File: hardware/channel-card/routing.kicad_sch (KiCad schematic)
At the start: 37 parts, among them J301 AUX1 PRE 1-3/2-4, POST 3-5/4-6, J302 AUX2 PRE 1-3/2-4, POST 3-5/4-6, Q301 MMBT3904, SW301 PFL (latching), SW302 SC SEND (latching), SW303 COMP BUS (latching), U301 NE5532, U302 DG413DY, U303 DG412DY

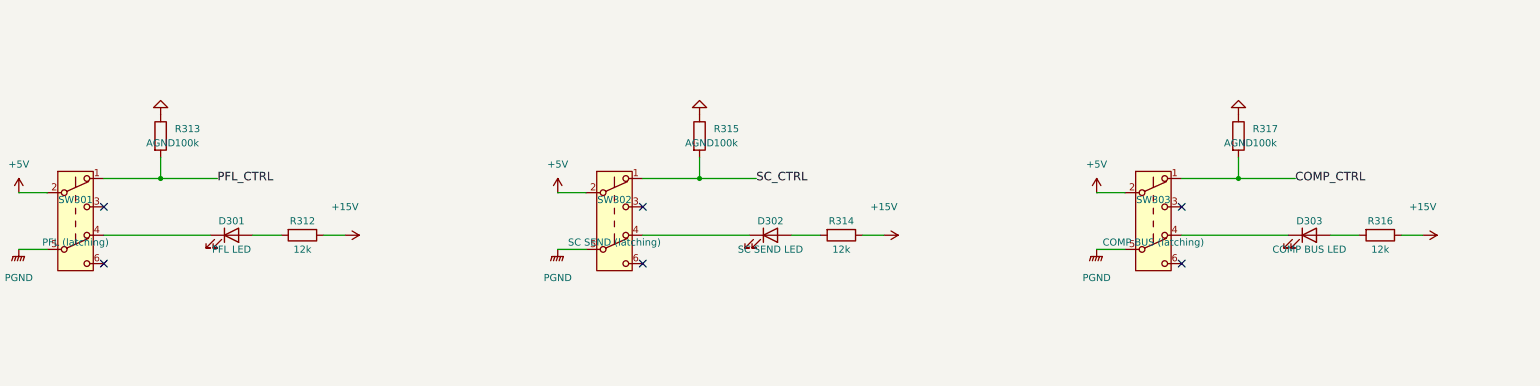
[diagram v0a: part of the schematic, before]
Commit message: Choose GPBS850N latching buttons with printed light caps
Buttons are CW Industries GPBS850N latching DPDT switches (Electrokit)
with 0805 LEDs lighting 3D-printed translucent caps (decision 75).
The datasheet shows pins 2-3 and 5-6 close when pressed, so every
button now uses pin 3 for logic and pin 6 for the LED. Adds the switch
footprint library, rebuild_all.sh, the state-retention requirement for
the momentary-button backlog item, and ten switches to the second
Electrokit order.

Co-Authored-By: Claude Opus 5.5 <noreply@anthropic.com>
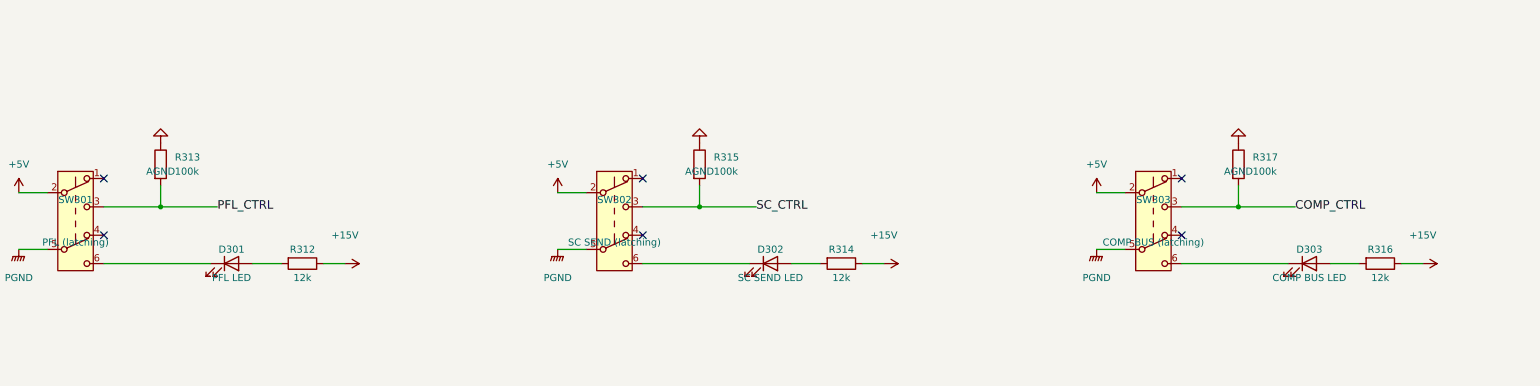
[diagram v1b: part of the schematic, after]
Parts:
- D301, D302, D303: footprint LED_THT:LED_D3.0mm -> LED_SMD:LED_0805_2012Metric
- SW301, SW302, SW303: footprint (none) -> syntsamix:SW_Latching_8.5x8.5mm_CW_GPBS850N; MPN (none) -> GPBS850N; Manufacturer (none) -> CW Industries; Supplier (none) -> Electrokit; SupplierPN (none) -> 41012905
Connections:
- net COMP_CTRL: now also SW303.3 (C); no longer SW303.1 (A)
- net PFL_CTRL: now also SW301.3 (C); no longer SW301.1 (A)
- net SC_CTRL: now also SW302.3 (C); no longer SW302.1 (A)
- net at SW301.4 (A): no longer D301.1 (K)
- net at D303.1 (K): now also SW303.6 (C); no longer SW303.4 (A)
- net at D302.1 (K): now also SW302.6 (C); no longer SW302.4 (A)
- net at SW301.6 (C): now also D301.1 (K)

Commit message: Add test pads to the channel card sheets
24 bare 1.5 mm test pads on key audio, control and ground nets across
the Input, Filter, Level, Routing and Meter sheets, named by net and
kept out of the BOM (decision 77). Each pad is in the reference
netlists, so the checks prove it sits on the intended net.

Co-Authored-By: Claude Opus 5.5 <noreply@anthropic.com>
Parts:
- added TP301: L_PRE, TestPoint:TestPoint_Pad_D1.5mm, symbol Connector:TestPoint
- added TP302: R_PRE, TestPoint:TestPoint_Pad_D1.5mm, symbol Connector:TestPoint
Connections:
- net L_PRE: now also TP301.1
- net R_PRE: now also TP302.1

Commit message: Check parts against LCSC stock and use basic resistor values
tools/lcsc_check.py checks docs/parts.csv against the JLCPCB/LCSC
catalogue and writes docs/lcsc-check.csv. Non-critical resistors move
to JLC basic values to cut setup fees (decision 79): bus resistors 22k,
VCA input network 100R, cutoff offset 470k, regulator dividers 200R/2k2
(15.1 V). All sheets rebuilt and verified (ERC 0/0).

Co-Authored-By: Claude Opus 5.5 <noreply@anthropic.com>
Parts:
- R301, R302, R303, R304, R307, R308, R309, R310: value 22k1 -> 22k; ProjectPN SX-R-033 -> SX-R-047

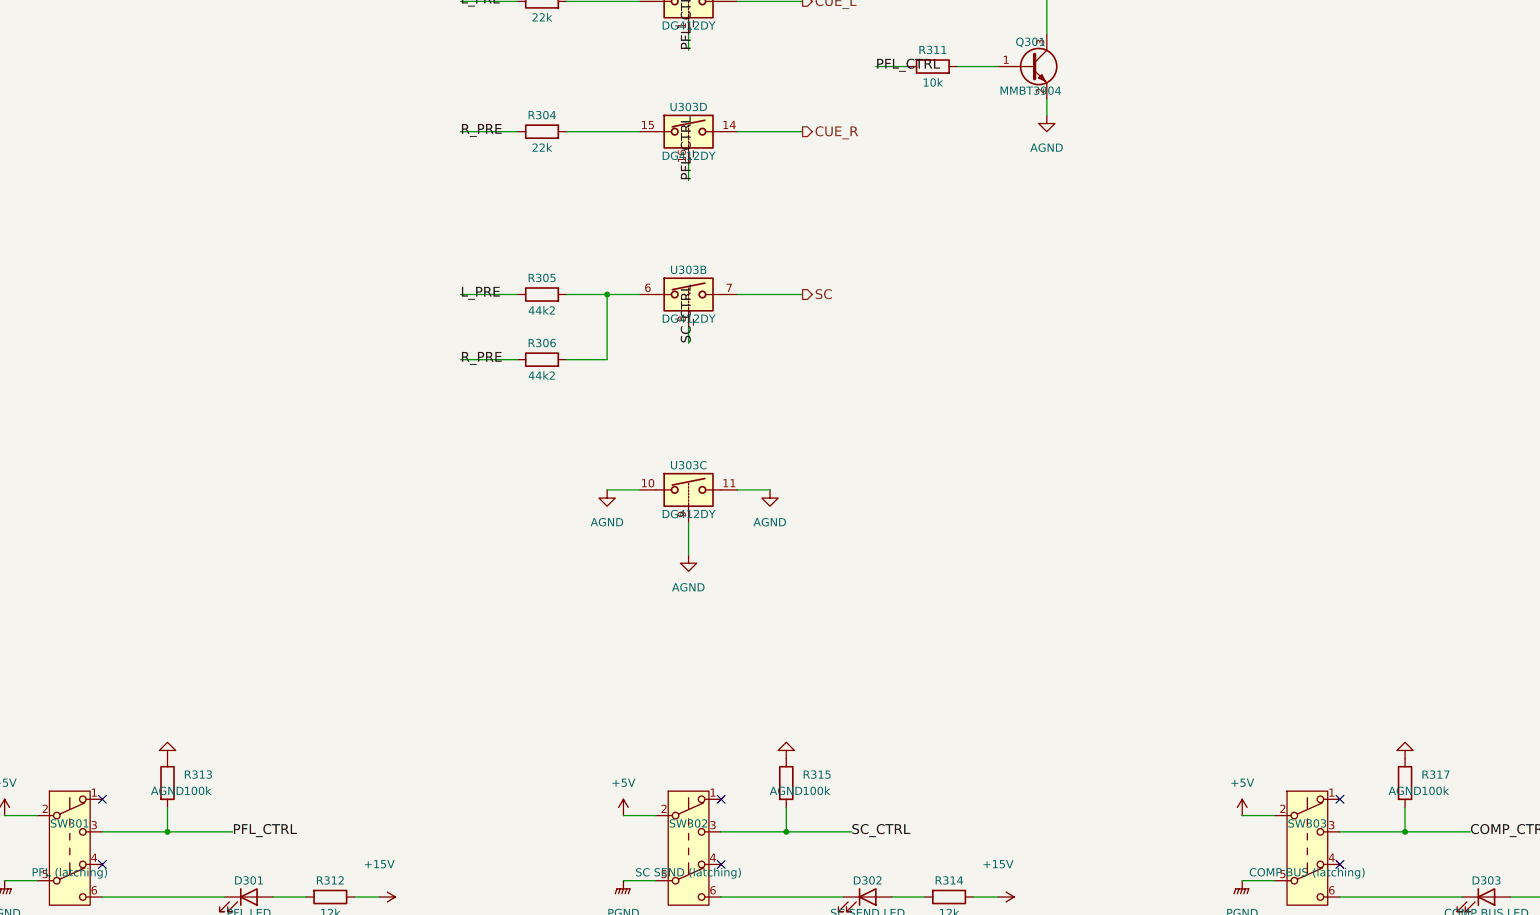
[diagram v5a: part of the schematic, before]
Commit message: Channel card: draw decisions 97 and 98, fader buffer on an OPA2171 (decision 102)
- Level: SC_ENV into the summer's virtual earth through R217 30k1, R218 removed,
  summer + input on AGND (decision 97)
- Q301 emitter and button pull-downs R17, R186, R220, R222, R313, R315, R317 to PGND (decision 98)
- U204 = OPA2171 for the fader buffer and control summer (input range includes V-);
  superdiodes moved to the TL072 U205 (decision 102)
- simulation/level: fader law within 1.2 dB, ducking 10.07 dB per -1 V at every fader position
- Power budget, parts list, STATUS, breadboard test 10 and working notes updated

Co-Authored-By: Claude Opus 5.5 <noreply@anthropic.com>
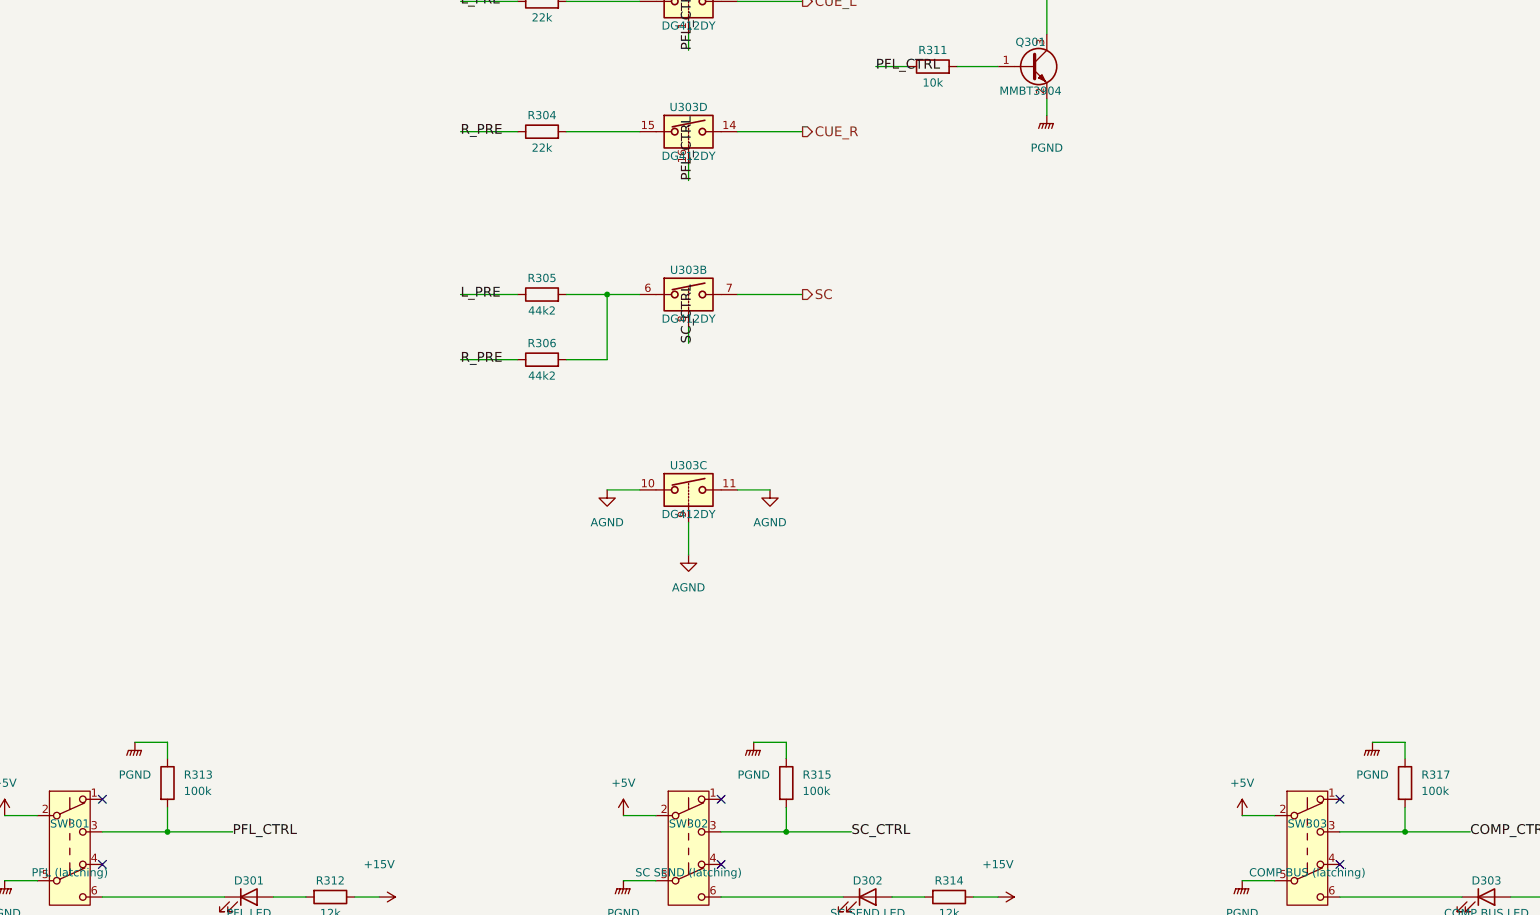
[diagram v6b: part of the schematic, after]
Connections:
- net AGND: no longer Q301.2 (E), R313.1, R315.1, R317.1
- net PGND: now also Q301.2 (E), R313.1, R315.1, R317.1

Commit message: Channel card: mechanical parts, decisions 110-117
- 110 LM317/LM337 in D2PAK on copper (onsemi, LCSC)
- 111 SMD electrolytics <= 5.4 mm (ROQANG, Panasonic bipolar)
- 112 trimmers and jumper headers on the underside, bottom cover for /system
- 113 low-cut caps C0G 1206
- 114 pot shaft standard T18 15 mm; 115 trim stage scaled to 100k, pots chosen
  (blocked until RoHS declarations)
- 116 RoHS strict for every part and board (process)
- 117 button LED colours (JLCPCB basic 0805), Wurth chain headers
- J181 drawn as Thonkiconn 3.5 mm (pending /system), fields and footprints set,
  five sheets rebuilt, netlists match, ERC 0/0
- STATUS: seven For /system items (CV jack, 0805 meter bezel, panel screws,
  bottom cover, underside keep-out, RoHS invariant, contract doc updates)

Co-Authored-By: Claude Opus 5.5 <noreply@anthropic.com>
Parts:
- D301: MPN (none) -> KT-0805Y; Manufacturer (none) -> Hubei KENTO; ProjectPN SX-D-002 -> SX-D-016; Supplier (none) -> LCSC; SupplierPN (none) -> C2296
- D302, D303: MPN (none) -> KT-0805G; Manufacturer (none) -> Hubei KENTO; ProjectPN SX-D-002 -> SX-D-011; Supplier (none) -> LCSC; SupplierPN (none) -> C2297
- RV301, RV302: ProjectPN SX-POT-005 -> SX-POT-013; Supplier (none) -> Thonk

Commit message: Channel card: pot MPNs on the symbols, R184 12k for the RESONANCE pot rating (decision 129)
- Alpha MPNs on RV1 (TRIM), RV181 (CUTOFF), RV301/RV302 (AUX); the Thonk
  -0057 variant suffix is left open
- RV183 reference netlist now SX-POT-012 (Tayda RD901F-40-15K-C10K),
  matching the drawing
- Decision 129: Alpha's RD901F spec rates non-B tapers at 0.02 W; RV183
  carried about 21 mW, R184 10k -> 12k gives about 17 mW (max Q current
  about 254 uA, provisional with R120/R170)
- RD901F spec facts in parts.csv; master STATUS notes RV402 RELEASE at
  about 20.2 mW for its own session

Netlists match, ERC 0/0.

Co-Authored-By: Claude Opus 5.5 <noreply@anthropic.com>
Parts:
- RV301, RV302: MPN (none) -> RD902F-40-15K-A10K-0057
